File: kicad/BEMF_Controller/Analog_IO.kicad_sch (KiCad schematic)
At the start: 29 parts, among them U10 OPA2376AIDR, U11 ADC108S022CIMTX/NOPB, U12 OPA2376AIDR

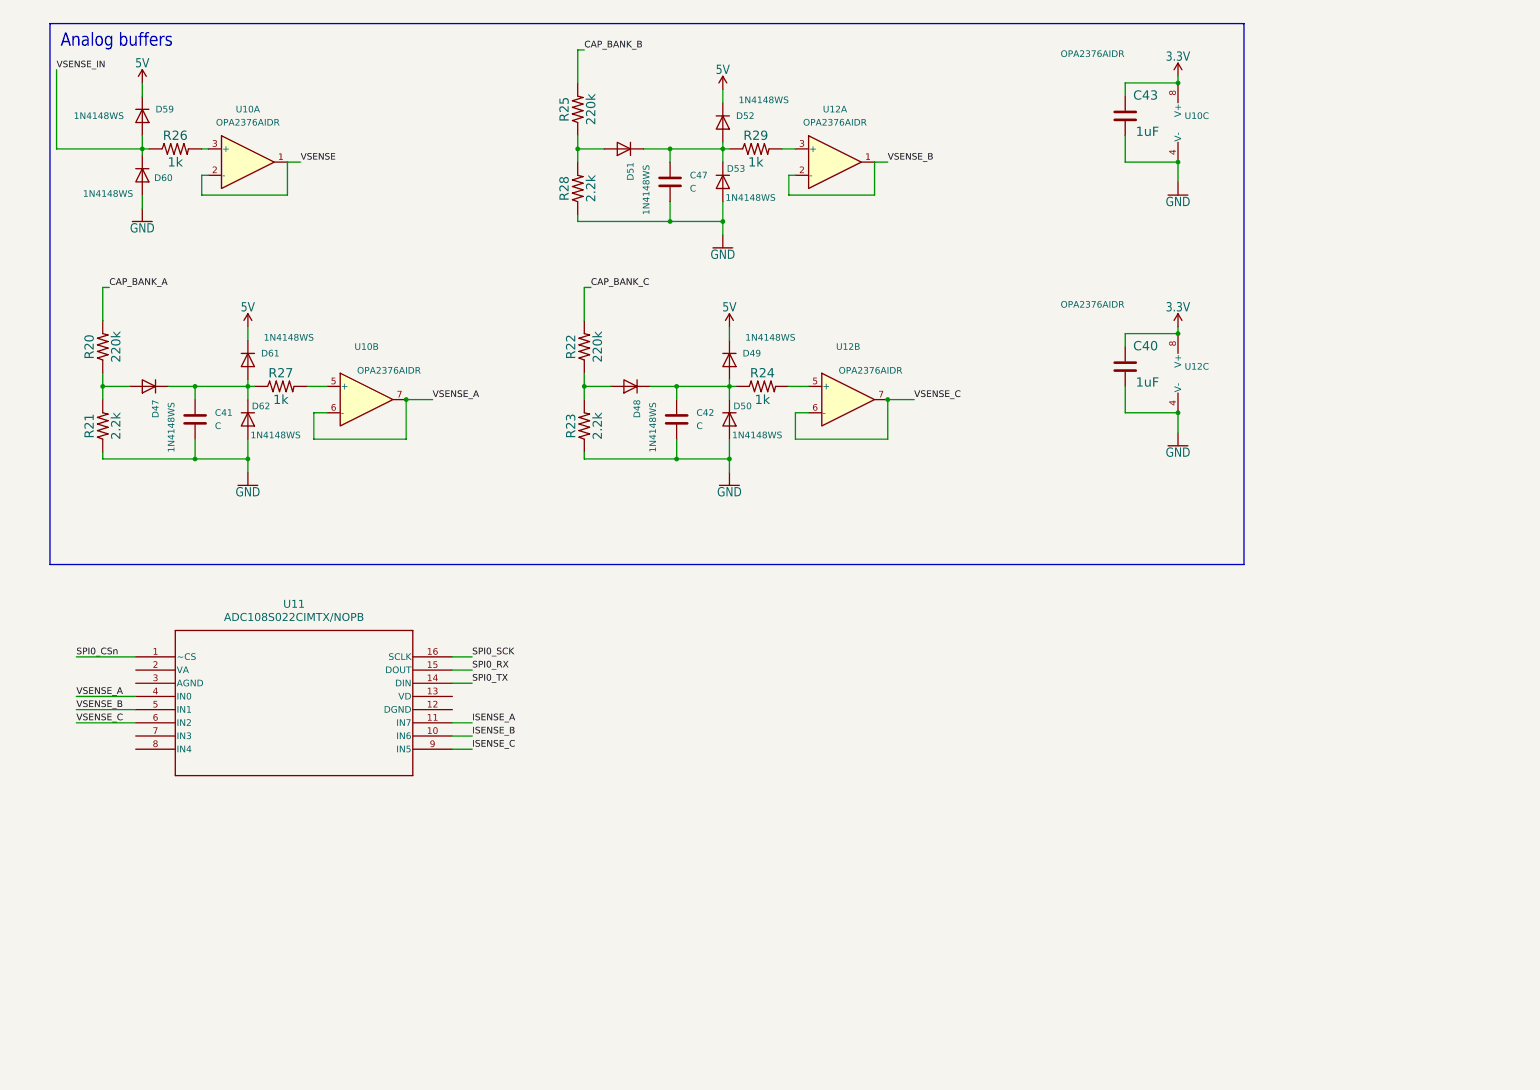
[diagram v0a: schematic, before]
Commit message: Several updates to analog section
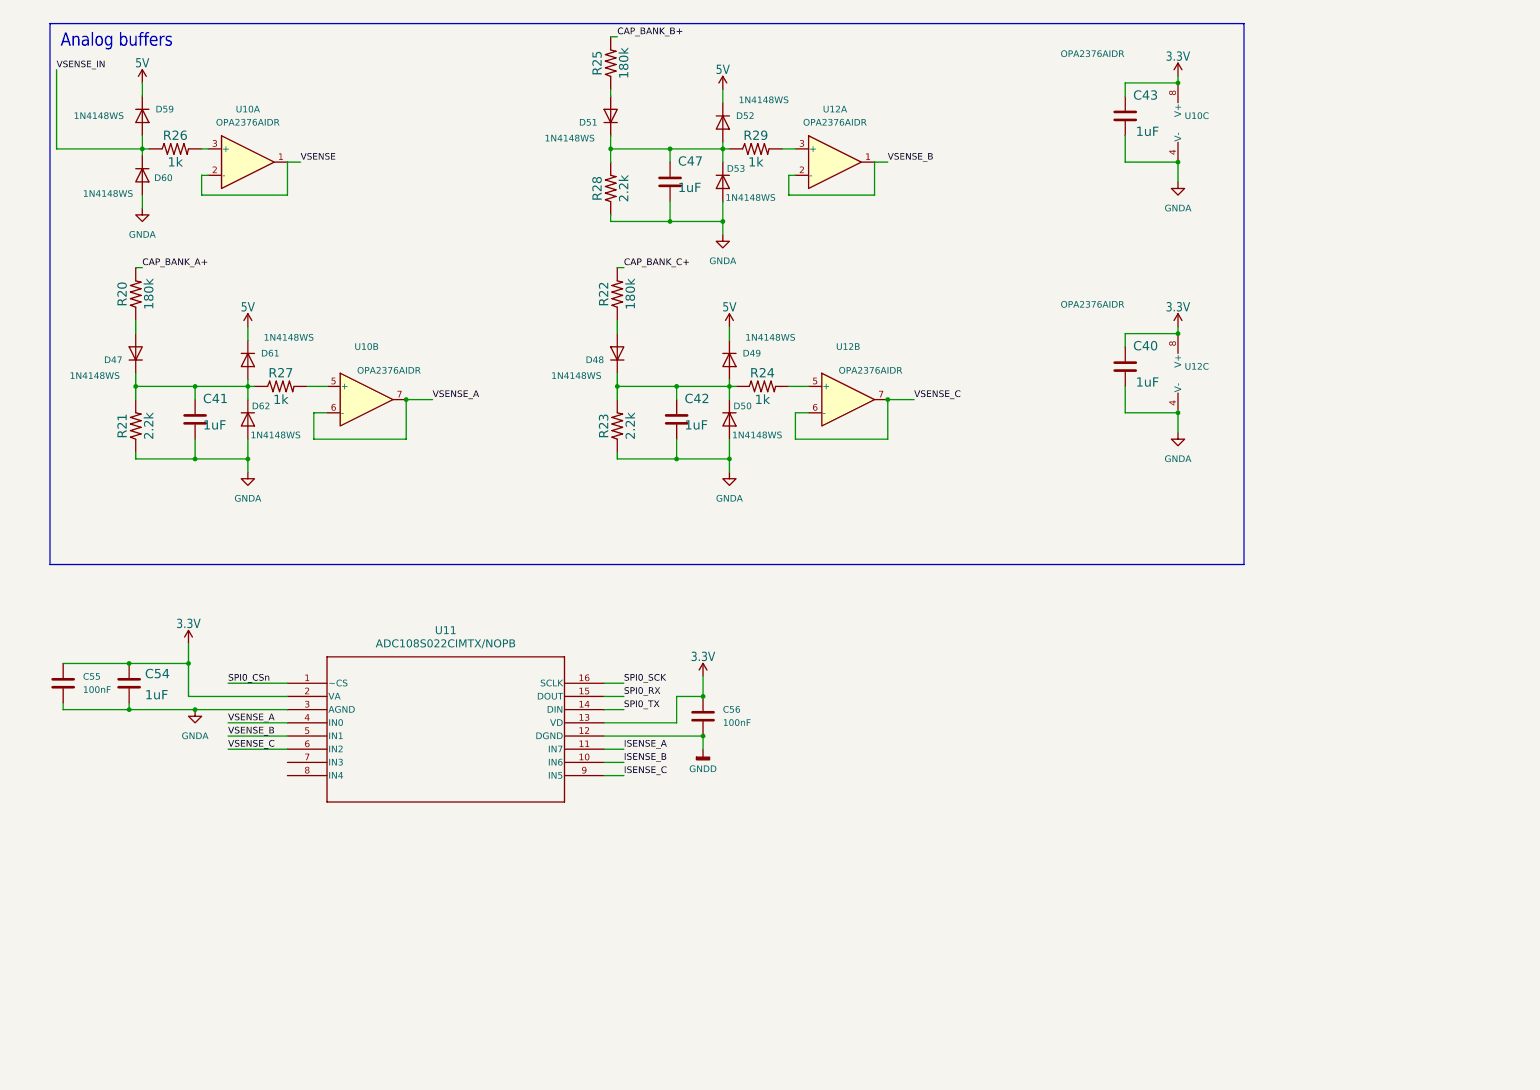
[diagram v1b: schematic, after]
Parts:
- removed C41, C42, C47: C, symbol Device:C
- added C41, C42, C47, C54: 1uF, Capacitor_SMD:C_1812_4532Metric, symbol Component_Library:CHV1812N250105MXT
- added C55, C56: 100nF, Capacitor_SMD:C_1210_3225Metric_Pad1.33x2.70mm_HandSolder, symbol Device:C
- R20, R22, R25: value 220k -> 180k
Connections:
- net GND is gone; now on net GNDA: C40.2, C43.2, D50.2 (A), D53.2 (A), D60.2 (A), D62.2 (A), R21.1, R23.1, R28.1, U10.4 (V-), U12.4 (V-)
- net 3.3V: now also U11.13 (VD), U11.2 (VA), C54.1, C55.1, C56.1
- net at D47.1 (K), D61.2 (A), D62.1 (K)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: now also R21.2, C41.1
- net at D48.2 (A), R22.1: no longer R23.2
- net at D51.2 (A), R25.1: no longer R28.2
- net at D51.1 (K), D52.2 (A), D53.1 (K)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: now also R28.2, C47.1
- net GNDD: now reaches U11.12 (DGND)
- net GNDD: now also C56.2
- net GNDA: now reaches U11.3 (AGND)
- net GNDA: now also C41.2, C42.2, C47.2, C54.2, C55.2
- net at D48.1 (K), D49.2 (A), D50.1 (K)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: now also R23.2, C42.1
- net at D47.2 (A), R20.1: no longer R21.2
- net CAP_BANK_A renamed CAP_BANK_A+
- net CAP_BANK_B renamed CAP_BANK_B+
- net CAP_BANK_C renamed CAP_BANK_C+
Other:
- moved on the sheet: D47, R20, R21, U11

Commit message: First version of PCB layout.
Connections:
- net GNDA: no longer C41.2, C42.2, C47.2, D50.2 (A), D53.2 (A), D60.2 (A), D62.2 (A), R21.1, R23.1, R28.1
- net VSENSE_A_IN: now reaches C41.1, D47.1 (K), D61.2 (A), D62.1 (K), R21.2, R27.1
- net VSENSE_C_IN: now reaches C42.1, D48.1 (K), D49.2 (A), D50.1 (K), R23.2, R24.1
- net VSENSE_B_IN: now reaches C47.1, D51.1 (K), D52.2 (A), D53.1 (K), R28.2, R29.1
- net GNDD renamed GND
- net GND: now also D60.2 (A)
- new net CAP_BANK_GND: C41.2, C42.2, C47.2, D50.2 (A), D53.2 (A), D62.2 (A), R21.1, R23.1, R28.1

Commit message: Feature complete, zero eroors in pcb. Still lot of warnings.
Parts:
- added C61, C63: 1uF, Capacitor_SMD:C_1812_4532Metric, symbol Component_Library:CHV1812N250105MXT
- added D54, D55, D56: 1N4148WS, Diode_SMD:D_SOD-323, symbol Diode:1N4148WS
- added JP10, JP8, JP9: SolderJumper_3_Bridged12, Jumper:SolderJumper-3_P1.3mm_Bridged2Bar12_RoundedPad1.0x1.5mm, symbol Jumper:SolderJumper_3_Bridged12
- added R41: 192k, main:1206, symbol main-eagle-import:RESISTOR1206
- added R42: 2.2k, main:1206, symbol main-eagle-import:RESISTOR1206
- added R43: 1k, main:1206, symbol main-eagle-import:RESISTOR1206
- added U16: OPA2376AIDR, footprints:D8, symbol Component_Library:OPA2376AIDR
- R20, R22, R25: value 180k -> 192k
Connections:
- net 3.3V: now also C63.1, U16.8 (V+)
- net 5V: now also D55.1 (K)
- net GND: now also C61.2, D56.2 (A), R42.1
- net GNDA: now also C63.2, U16.4 (V-)
- net ISENSE_A: now also JP8.3 (B); no longer U11.11 (IN7)
- net ISENSE_B: now also JP9.3 (B); no longer U11.10 (IN6)
- net ISENSE_C: now also JP10.3 (B); no longer U11.9 (IN5)
- net VSENSE: now also U11.7 (IN3)
- net VSENSE_L: now reaches U11.8 (IN4)
- net VSENSE_L: now also U16.6 (-), U16.7
- new net: D54.2 (A), R41.1
- new net: R43.2, U16.5 (+)
- new net DUTY: U11.11 (IN7)
- new net HALL_1: JP8.1 (A)
- new net HALL_2: JP9.1 (A)
- new net HALL_3: JP10.1 (A)
- new net ISENSE: U11.9 (IN5)
- new net ISENSE_A_HALL_1: JP8.2 (C)
- new net ISENSE_B_HALL_2: JP9.2 (C)
- new net ISENSE_C_HALL_3: JP10.2 (C)
- new net LOAD+: R41.2
- new net THROTTLE: U11.10 (IN6)
- new net VSENSE_L_IN: C61.1, D54.1 (K), D55.2 (A), D56.1 (K), R42.2, R43.1
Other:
- moved on the sheet: C54, C55, C56, U11

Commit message: Added analog Hall inputs and worked away lot of warnings.
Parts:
- U11: footprint MTC16 -> footprints:MTC16
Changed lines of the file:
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@@
 			)
 		)
-		(property "Footprint" "MTC16"
+		(property "Footprint" "footprints:MTC16"
 			(at 50.8 184.15 0)
 			(effects
@@
 			)
 		)
-		(property "Datasheet" "https://www.ti.com/lit/ds/symlink/adc108s022.pdf"
+		(property "Datasheet" "ADC108S022CIMTX/NOPB"
 			(at 50.8 184.15 0)
 			(effects

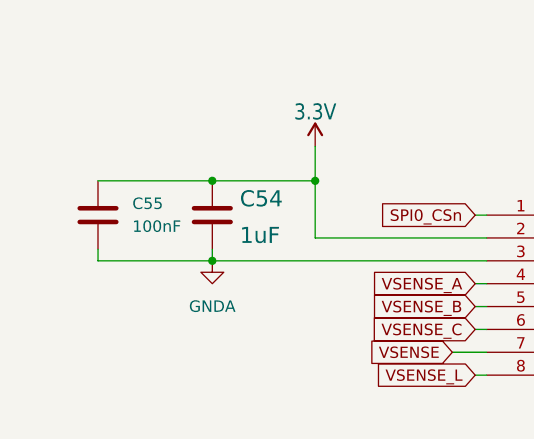
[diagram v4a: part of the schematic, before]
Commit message: Simplification, high and low side driven together.
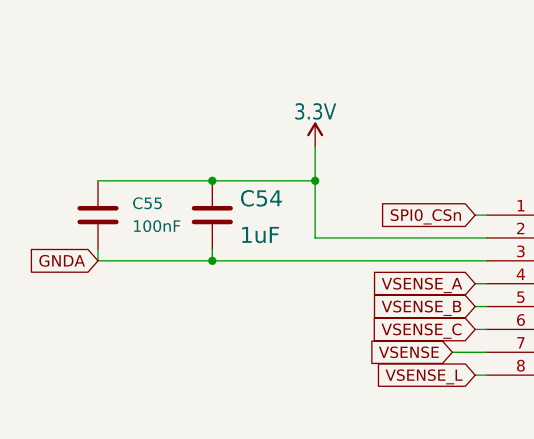
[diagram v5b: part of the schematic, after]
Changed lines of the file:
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@@
 		)
 	)
+	(global_label "GNDA"
+		(shape input)
+		(at 7.62 189.23 180)
+		(fields_autoplaced yes)
+		(effects
+			(font
+				(size 1.27 1.27)
+			)
+			(justify right)
+		)
+		(property "Intersheetrefs" "${INTERSHEET_REFS}"
+			(at -0.3243 189.23 0)
+			(effects
+				(font
+					(size 1.27 1.27)
+				)
+				(justify right)
+				(hide yes)
+			)
+		)
+	)
 	(global_label "SPI0_RX"
 		(shape input)
@@
 					(unit 1)
 				)
-			)
-		)
-	)
-	(symbol
-		(lib_id "power:GNDA")
-		(at 20.32 189.23 0)
-		(unit 1)
-		(exclude_from_sim no)
-		(in_bom yes)
-		(on_board yes)
-		(dnp no)
-		(fields_autoplaced yes)
-		(property "Reference" "#PWR01"
-			(at 20.32 195.58 0)
-			(effects
-				(font
-					(size 1.27 1.27)
-				)
-				(hide yes)
-			)
-		)
-		(property "Value" "GNDA"
-			(at 20.32 194.31 0)
-			(effects
-				(font
-					(size 1.27 1.27)
-				)
-			)
-		)
-		(property "Footprint" ""
-			(at 20.32 189.23 0)
-			(effects
-				(font
-					(size 1.27 1.27)
-				)
-				(hide yes)
-			)
-		)
-		(property "Datasheet" ""
-			(at 20.32 189.23 0)
-			(effects
-				(font
-					(size 1.27 1.27)
-				)
-				(hide yes)
-			)
-		)
-		(property "Description" "Power symbol creates a global label with name \"GNDA\" , analog ground"
-			(at 20.32 189.23 0)
-			(effects
-				(font
-					(size 1.27 1.27)
-				)
-				(hide yes)
-			)
-		)
-		(pin "1"
-		)
-		(instances
-			(project "BEMF_Controller"
-				(path "/80a514a6-29a9-4699-8a7d-cff678a7ed07/6990bf25-70eb-45d9-b265-2461b625100e"
-					(reference "#PWR01")
-					(unit 1)
-				)

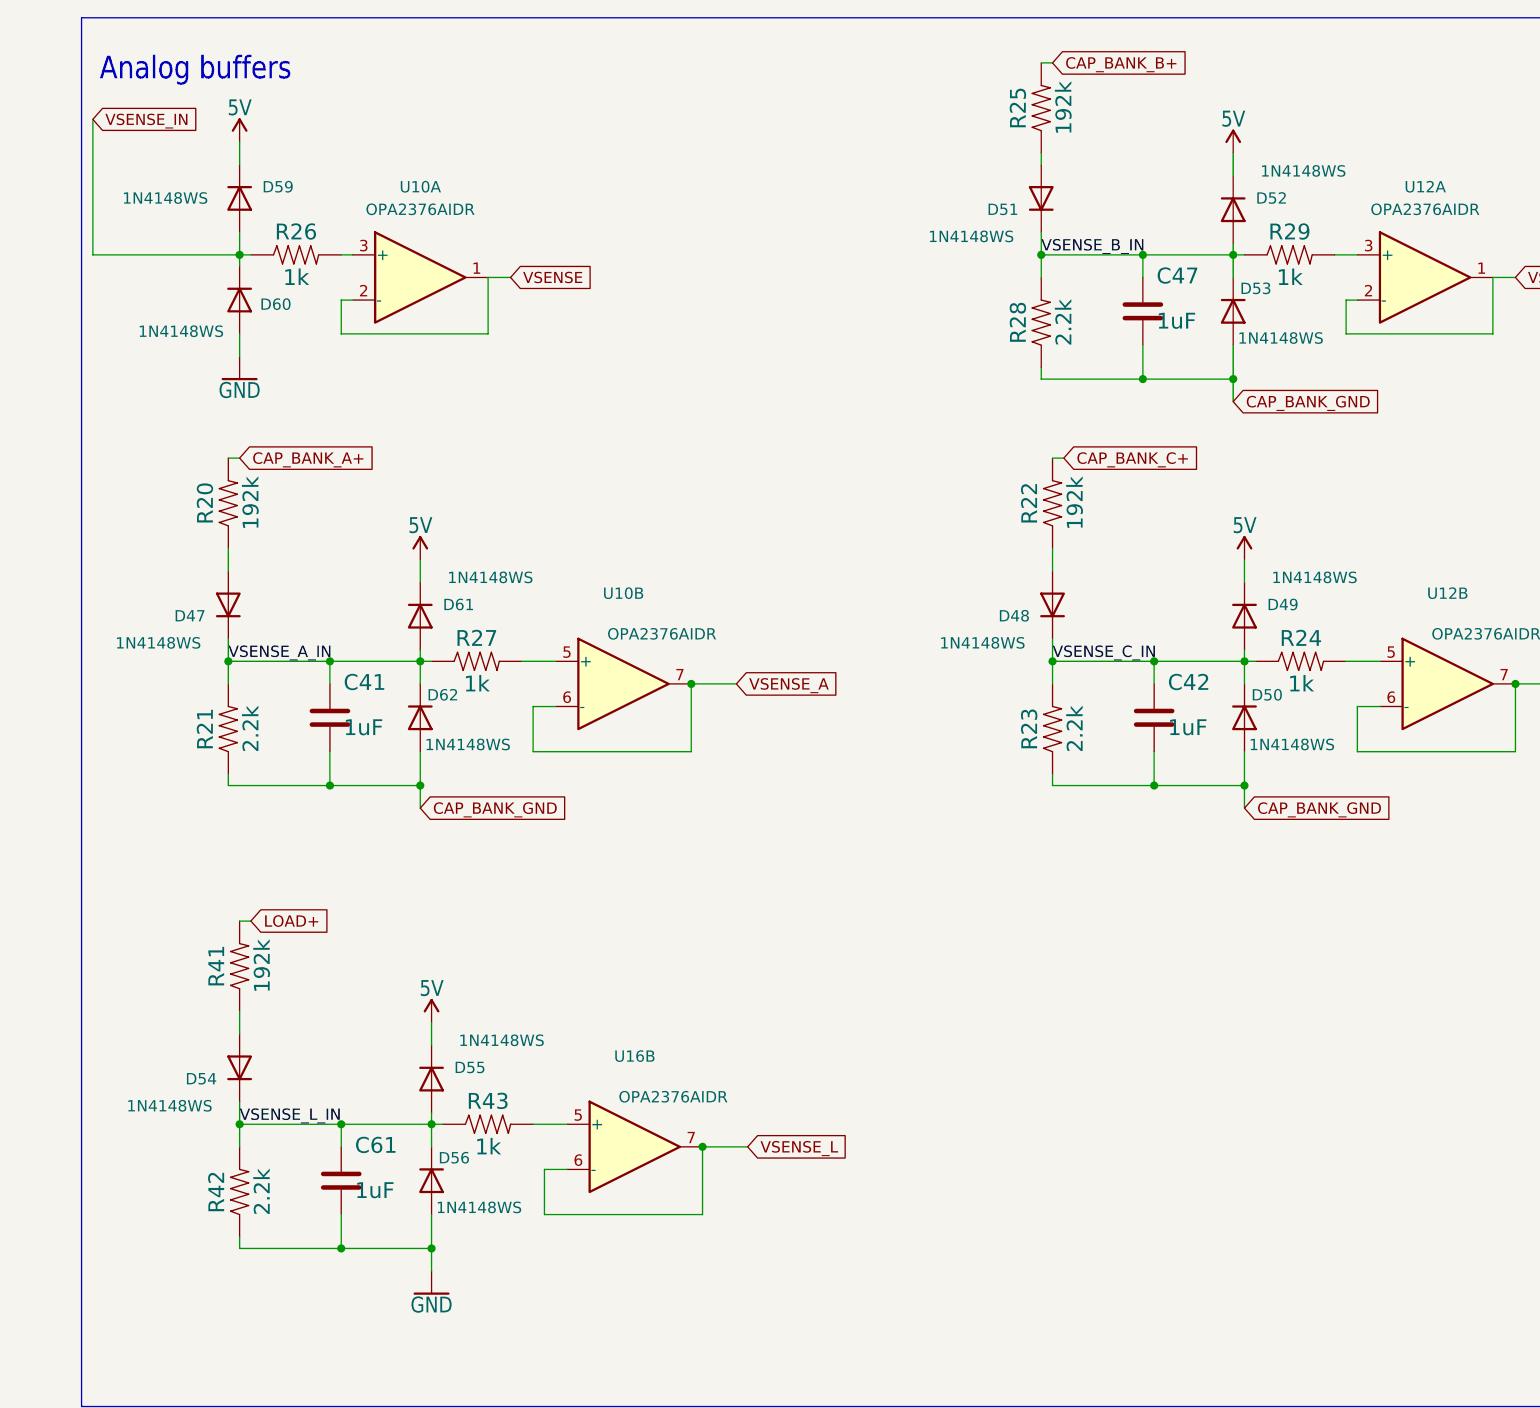
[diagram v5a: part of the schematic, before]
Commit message: Fixed all warnings.
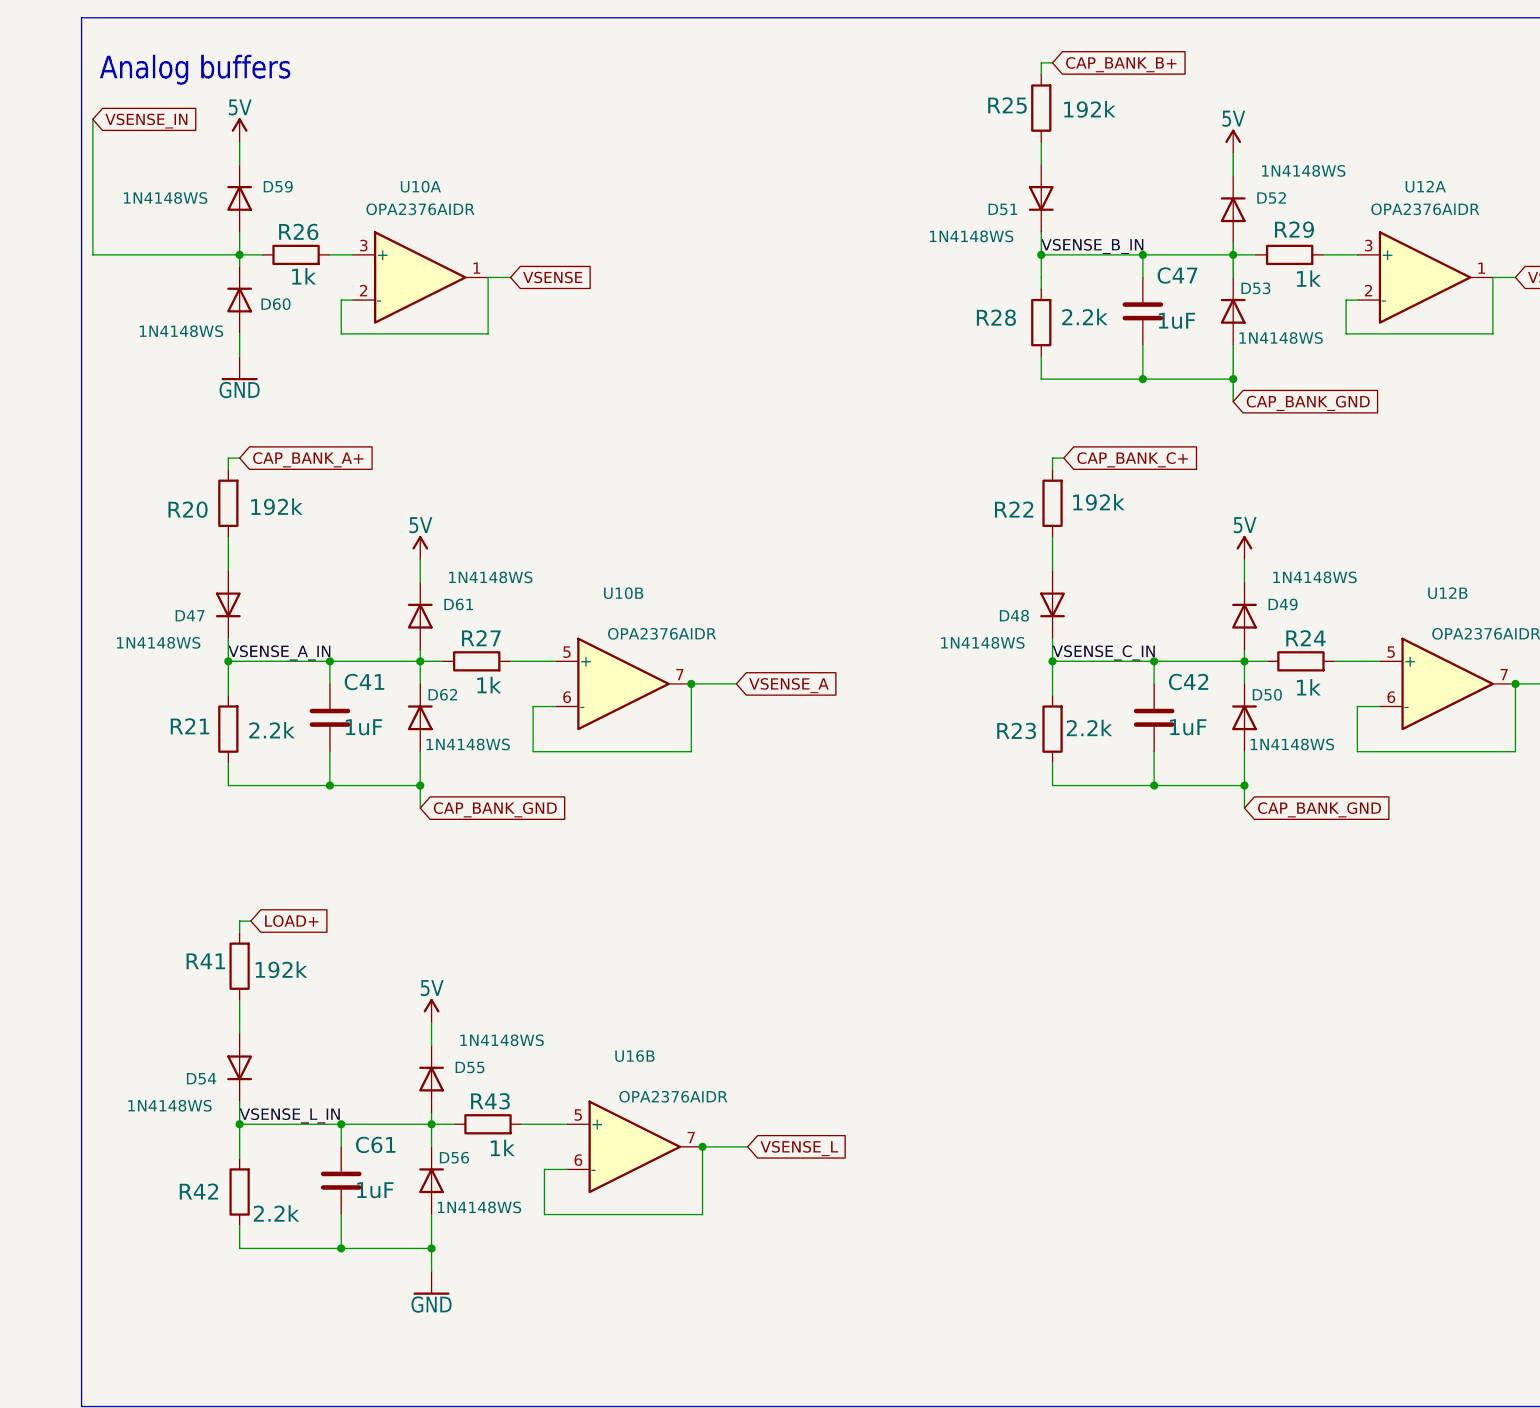
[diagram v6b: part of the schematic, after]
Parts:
- R20, R22, R25, R41: footprint main:1206 -> Resistor_SMD:R_1206_3216Metric; symbol main-eagle-import:RESISTOR1206 -> Component_Library:R192k
- R21, R23, R28, R42: footprint main:1206 -> Resistor_SMD:R_1206_3216Metric; symbol main-eagle-import:RESISTOR1206 -> Component_Library:R2k2
- R24, R26, R27, R29, R43: footprint main:1206 -> Resistor_SMD:R_1206_3216Metric; symbol main-eagle-import:RESISTOR1206 -> Component_Library:R1k
